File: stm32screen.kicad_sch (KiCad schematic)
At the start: 43 parts, among them J2 GC9A01, J3 Oil temp sensor, J4 pressure sensor, J5 USB_B_Micro, J6 EGT_sensor, SW1 SW_Push, SW2 SW_Push, U1 TS1117BCW-3.3, U2 STM32F407VETx, U3 MAX31856

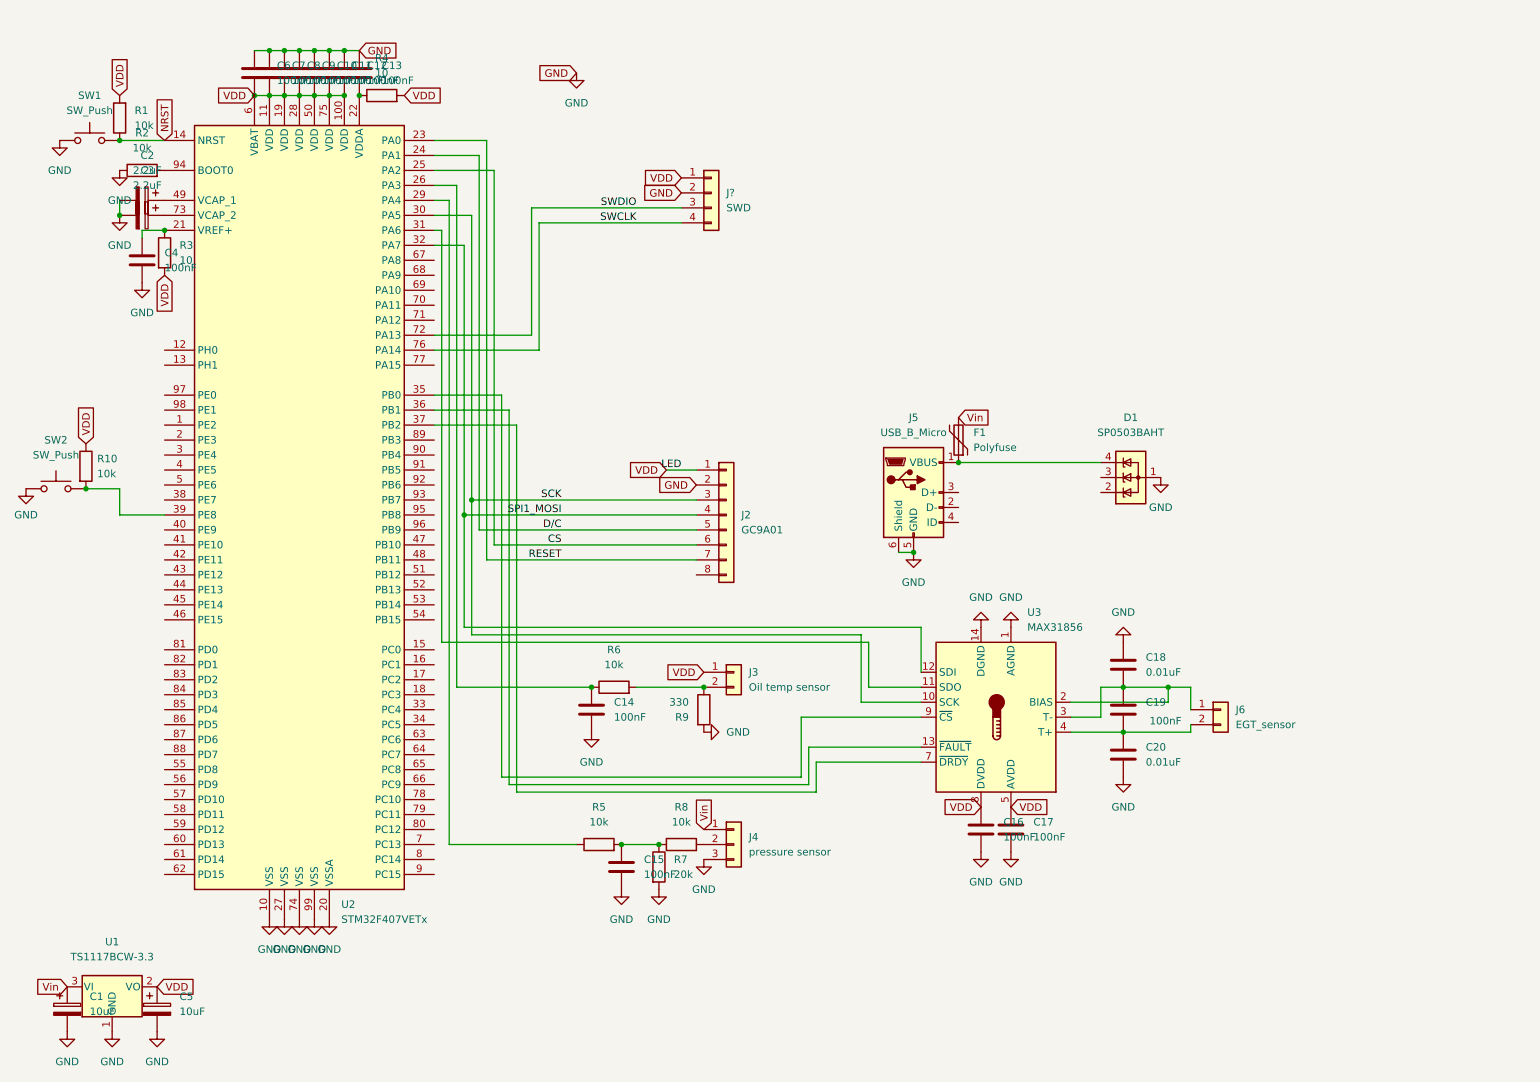
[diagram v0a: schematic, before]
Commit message: Roughing out the PCB.
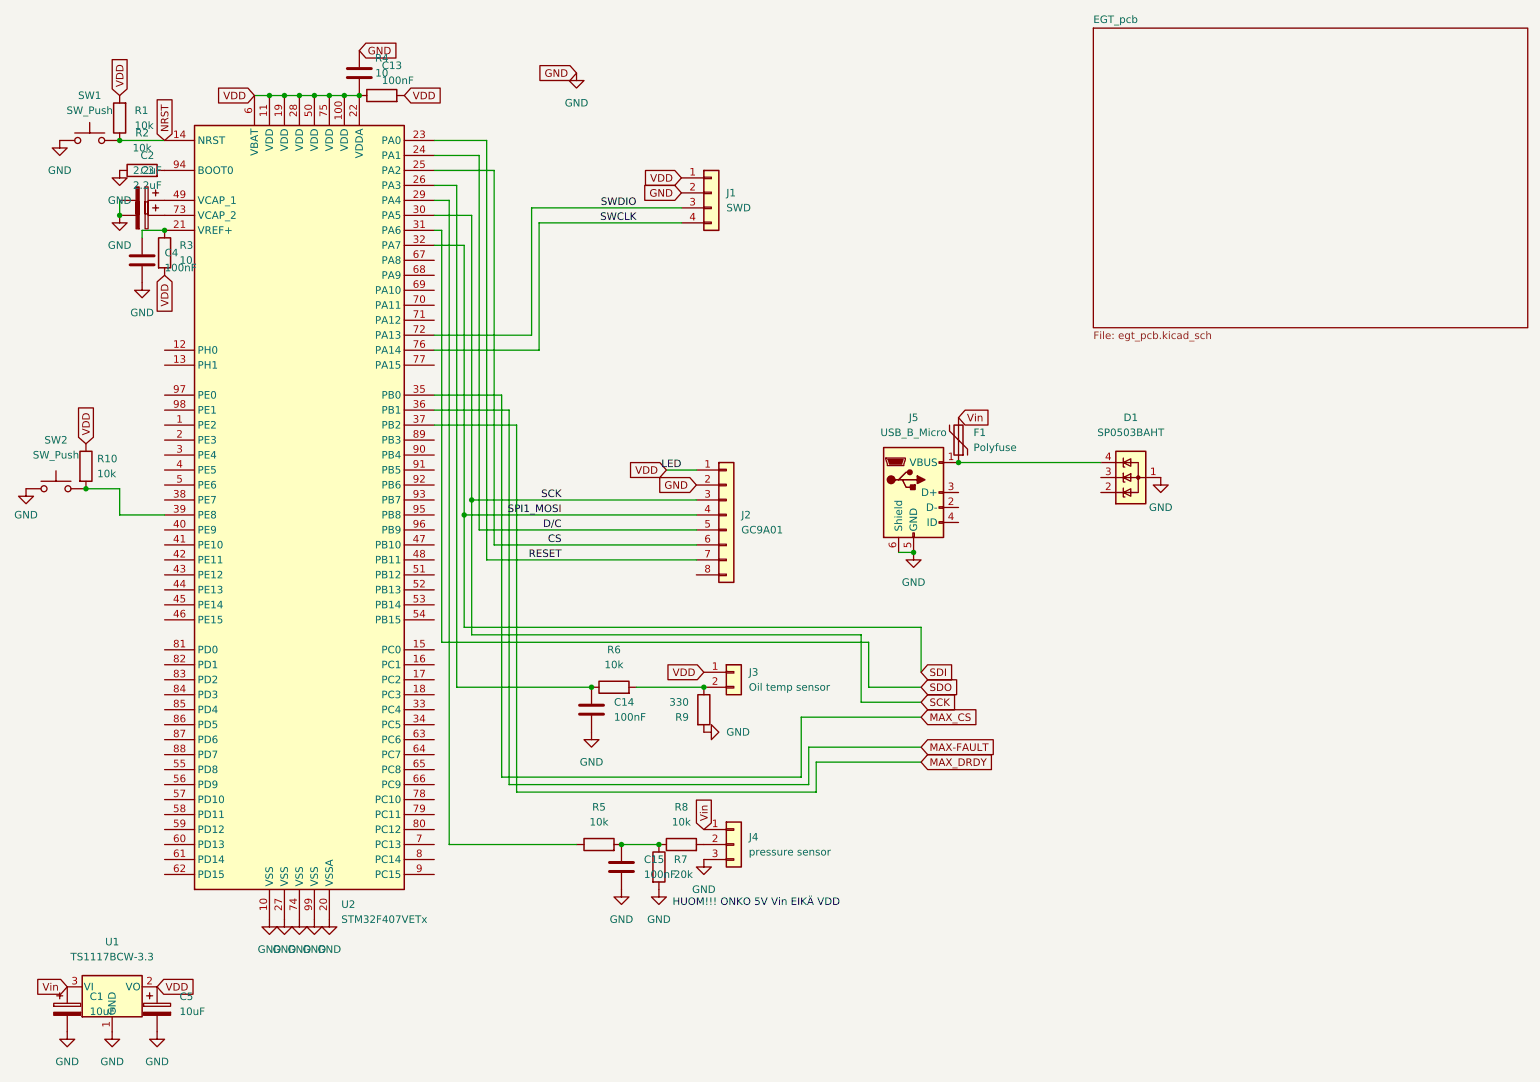
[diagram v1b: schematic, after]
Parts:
- removed C10, C11, C12, C16, C17, C19, C6, C7, C8, C9: 100nF, Capacitor_SMD:C_0805_2012Metric_Pad1.18x1.45mm_HandSolder, symbol Device:C
- removed C18, C20: 0.01uF, Capacitor_SMD:C_0402_1005Metric_Pad0.74x0.62mm_HandSolder, symbol Device:C
- removed J6: EGT_sensor, Connector_JST:JST_XH_B2B-XH-A_1x02_P2.50mm_Vertical, symbol Connector_Generic:Conn_01x02
- removed U3: MAX31856, Package_SO:TSSOP-14_4.4x5mm_P0.65mm, symbol Sensor_Temperature:MAX31856
- gave numbers to parts that had none: 1
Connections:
- net VDD: now also C13.2, R4.1, U2.22 (VDDA)
- net SDO: now reaches U2.31 (PA6)
- net MAX_CS: now reaches U2.35 (PB0)
- net MAX-FAULT: now reaches U2.36 (PB1)
- net MAX_DRDY: now reaches U2.37 (PB2)
- net SPI1_MOSI renamed SDI
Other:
- added sheet EGT_pcb (egt_pcb.kicad_sch)
- note added: "HUOM!!! ONKO 5V Vin EIKÄ VDD"

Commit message: Added a status LED
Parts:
- added D2: LED, LED_SMD:LED_0603_1608Metric_Pad1.05x0.95mm_HandSolder, symbol Device:LED
- added R11: 68, Resistor_SMD:R_0603_1608Metric_Pad0.98x0.95mm_HandSolder, symbol Device:R
- J1: footprint (none) -> Connector_PinHeader_2.54mm:PinHeader_1x04_P2.54mm_Vertical
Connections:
- net GND: now also R11.1
- net VDD: now also D2.2 (A)
- new net: D2.1 (K), R11.2
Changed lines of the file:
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@@
+		)
+	)
+	(global_label "GND"
+		(shape input)
+		(at 130.81 72.39 180)
+		(fields_autoplaced yes)
+		(effects
+			(font
+				(size 1.27 1.27)
+			)
+			(justify right)
+		)
+		(property "Intersheetrefs" "${INTERSHEET_REFS}"
+			(at 123.9543 72.39 0)
+			(effects
+				(font
+					(size 1.27 1.27)
+				)
+				(justify right)
+				(hide yes)
+			)
 		)
 	)
@@
 		)
 	)
+	(global_label "VDD"
+		(shape input)
+		(at 146.05 72.39 0)
+		(fields_autoplaced yes)
+		(effects
+			(font
+				(size 1.27 1.27)
+			)
+			(justify left)
+		)
+		(property "Intersheetrefs" "${INTERSHEET_REFS}"
+			(at 152.6638 72.39 0)
+			(effects
+				(font
+					(size 1.27 1.27)
+				)
+				(justify left)
+				(hide yes)
+			)
+		)
+	)
 	(global_label "SDO"
 		(shape input)
@@
 			)
 		)
-		(property "Footprint" ""
+		(property "Footprint" "Connector_PinHeader_2.54mm:PinHeader_1x04_P2.54mm_Vertical"
 			(at 134.62 43.18 0)
 			(effects
@@
 	)
 	(symbol
+		(lib_id "Device:LED")
+		(at 142.24 72.39 0)
+		(unit 1)
+		(exclude_from_sim no)
+		(in_bom yes)
+		(on_board yes)
+		(dnp no)
+		(fields_autoplaced yes)
+		(property "Reference" "D2"
+			(at 140.6525 66.04 0)
+			(effects
+				(font
+					(size 1.27 1.27)
+				)
+			)
+		)
+		(property "Value" "LED"
+			(at 140.6525 68.58 0)
+			(effects
+				(font
+					(size 1.27 1.27)
+				)
+			)
+		)
+		(property "Footprint" "LED_SMD:LED_0603_1608Metric_Pad1.05x0.95mm_HandSolder"
+			(at 142.24 72.39 0)
+			(effects
+				(font
+					(size 1.27 1.27)
+				)
+				(hide yes)
+			)
+		)
+		(property "Datasheet" "~"
+			(at 142.24 72.39 0)
+			(effects
+				(font
+					(size 1.27 1.27)
+				)
+				(hide yes)
+			)
+		)
+		(property "Description" "Light emitting diode"
+			(at 142.24 72.39 0)
+			(effects
+				(font
+					(size 1.27 1.27)
+				)
+				(hide yes)
+			)
+		)
+		(property "Sim.Pins" "1=K 2=A"
+			(at 142.24 72.39 0)
+			(effects
+				(font
+					(size 1.27 1.27)
+				)
+				(hide yes)
+			)
+		)
+		(pin "1"
+		)
+		(pin "2"
+		)
+		(instances
+			(project ""
+				(path "/dd9634c9-b7ae-401f-800b-241ca4b8e751"
+					(reference "D2")
+					(unit 1)
+				)
+			)
+		)
+	)
+	(symbol
 		(lib_id "power:GND")
 		(at 111.76 22.86 0)
@@
 					(unit 1)
 				)
+			)
+		)
+	)
+	(symbol
+		(lib_id "Device:R")
+		(at 134.62 72.39 90)
+		(unit 1)
+		(exclude_from_sim no)
+		(in_bom yes)
+		(on_board yes)
+		(dnp no)
+		(fields_autoplaced yes)
+		(property "Reference" "R11"
+			(at 134.62 66.04 90)
+			(effects
+				(font
+					(size 1.27 1.27)
+				)
+			)
+		)
+		(property "Value" "68"
+			(at 134.62 68.58 90)
+			(effects
+				(font
+					(size 1.27 1.27)
+				)
+			)
+		)
+		(property "Footprint" "Resistor_SMD:R_0603_1608Metric_Pad0.98x0.95mm_HandSolder"
+			(at 134.62 74.168 90)
+			(effects
+				(font
+					(size 1.27 1.27)
+				)
+				(hide yes)
+			)
+		)
+		(property "Datasheet" "~"
+			(at 134.62 72.39 0)
+			(effects
+				(font
+					(size 1.27 1.27)
+				)
+				(hide yes)
+			)
+		)
+		(property "Description" "Resistor"
+			(at 134.62 72.39 0)
+			(effects
+				(font
+					(size 1.27 1.27)
+				)
+				(hide yes)
+			)
+		)
+		(pin "1"
+		)
+		(pin "2"
+		)
+		(instances
+			(project ""
+				(path "/dd9634c9-b7ae-401f-800b-241ca4b8e751"
+					(reference "R11")
+					(unit 1)
+				)

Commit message: Optimized PCB layout. Added images
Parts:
- J2: footprint Connector_PinHeader_2.54mm:PinHeader_1x08_P2.54mm_Vertical -> Connector_JST:JST_PH_B7B-PH-K_1x07_P2.00mm_Vertical
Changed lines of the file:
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@@
+	)
+	(junction
+		(at 187.96 88.9)
+		(diameter 0)
+		(color 0 0 0 0)
 	)
 	(junction
@@
 	(wire
 		(pts
+			(xy 187.96 88.9) (xy 200.66 88.9)
+		)
+		(stroke
+			(width 0)
+			(type default)
+		)
+	)
+	(wire
+		(pts
 			(xy 160.02 129.54) (xy 160.02 118.11)
 		)
@@
 	(wire
 		(pts
-			(xy 176.53 88.9) (xy 200.66 88.9)
+			(xy 187.96 80.01) (xy 187.96 88.9)
+		)
+		(stroke
+			(width 0)
+			(type default)
+		)
+	)
+	(wire
+		(pts
+			(xy 176.53 88.9) (xy 187.96 88.9)
 		)
 		(stroke
@@
 			)
 		)
-		(property "Footprint" "Connector_PinHeader_2.54mm:PinHeader_1x08_P2.54mm_Vertical"
+		(property "Footprint" "Connector_JST:JST_PH_B7B-PH-K_1x07_P2.00mm_Vertical"
 			(at 137.16 97.79 0)
 			(effects

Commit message: Changed PCB size to 23mm radius, rearranged parts to fit
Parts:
- removed J5: USB_B_Micro, Connector_USB:USB_Micro-B_Amphenol_10118194_Horizontal, symbol Connector:USB_B_Micro
- added J5: POWER IN, Connector_JST:JST_XH_B2B-XH-A_1x02_P2.50mm_Vertical, symbol Connector_Generic:Conn_01x02
- SW1: footprint Button_Switch_THT:SW_PUSH_6mm -> Button_Switch_SMD:SW_Push_1P1T_NO_CK_KSC9xxG
- SW2: footprint Connector_PinHeader_2.54mm:PinHeader_1x02_P2.54mm_Vertical -> Button_Switch_SMD:SW_Push_1P1T_NO_CK_KSC9xxG
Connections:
- net GND: now also J5.1 (Pin_1)
- net at D1.4 (K), F1.1: now also J5.2 (Pin_2)
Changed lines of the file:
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@@
 	)
 	(junction
-		(at 187.96 88.9)
-		(diameter 0)
-		(color 0 0 0 0)
-	)
-	(junction
 		(at 64.77 26.67)
 		(diameter 0)
@@
 	)
 	(junction
-		(at 168.91 104.14)
-		(diameter 0)
-		(color 0 0 0 0)
-	)
-	(junction
 		(at 67.31 26.67)
 		(diameter 0)
@@
 	(wire
 		(pts
-			(xy 187.96 88.9) (xy 200.66 88.9)
-		)
-		(stroke
-			(width 0)
-			(type default)
-		)
-	)
-	(wire
-		(pts
 			(xy 160.02 129.54) (xy 160.02 118.11)
 		)
@@
 	(wire
 		(pts
-			(xy 166.37 104.14) (xy 168.91 104.14)
-		)
-		(stroke
-			(width 0)
-			(type default)
-		)
-	)
-	(wire
-		(pts
 			(xy 161.29 119.38) (xy 161.29 127)
 		)
@@
 	(wire
 		(pts
-			(xy 88.9 119.38) (xy 161.29 119.38)
+			(xy 176.53 88.9) (xy 167.64 88.9)
 		)
 		(stroke
@@
 	(wire
 		(pts
-			(xy 187.96 80.01) (xy 187.96 88.9)
+			(xy 88.9 119.38) (xy 161.29 119.38)
 		)
 		(stroke
@@
 	(wire
 		(pts
-			(xy 176.53 88.9) (xy 187.96 88.9)
+			(xy 176.53 88.9) (xy 200.66 88.9)
 		)
 		(stroke
@@
 	(wire
 		(pts
+			(xy 167.64 88.9) (xy 167.64 90.17)
+		)
+		(stroke
+			(width 0)
+			(type default)
+		)
+	)
+	(wire
+		(pts
 			(xy 101.6 82.55) (xy 87.63 82.55)
 		)
@@
 	)
 	(symbol
-		(lib_id "Connector:USB_B_Micro")
-		(at 168.91 93.98 0)
-		(unit 1)
-		(exclude_from_sim no)
-		(in_bom yes)
-		(on_board yes)
-		(dnp no)
-		(fields_autoplaced yes)
-		(property "Reference" "J5"
-			(at 168.91 81.28 0)
-			(effects
-				(font
-					(size 1.27 1.27)
-				)
-			)
-		)
-		(property "Value" "USB_B_Micro"
-			(at 168.91 83.82 0)
-			(effects
-				(font
-					(size 1.27 1.27)
-				)
-			)
-		)
-		(property "Footprint" "Connector_USB:USB_Micro-B_Amphenol_10118194_Horizontal"
-			(at 172.72 95.25 0)
-			(effects
-				(font
-					(size 1.27 1.27)
-				)
-				(hide yes)
-			)
-		)
-		(property "Datasheet" "~"
-			(at 172.72 95.25 0)
-			(effects
-				(font
-					(size 1.27 1.27)
-				)
-				(hide yes)
-			)
-		)
-		(property "Description" ""
-			(at 168.91 93.98 0)
-			(effects
-				(font
-					(size 1.27 1.27)
-				)
-			)
-		)
-		(pin "1"
-		)
-		(pin "2"
-		)
-		(pin "3"
-		)
-		(pin "4"
-		)
-		(pin "5"
-		)
-		(pin "6"
-		)
-		(instances
-			(project ""
-				(path "/dd9634c9-b7ae-401f-800b-241ca4b8e751"
-					(reference "J5")
-					(unit 1)
-				)
-			)
-		)
-	)
-	(symbol
 		(lib_id "Switch:SW_Push")
 		(at 29.21 34.29 0)
@@
 			)
 		)
-		(property "Footprint" "Button_Switch_THT:SW_PUSH_6mm"
+		(property "Footprint" "Button_Switch_SMD:SW_Push_1P1T_NO_CK_KSC9xxG"
 			(at 29.21 29.21 0)
 			(effects
@@
 	(symbol
 		(lib_id "power:GND")
-		(at 168.91 104.14 0)
-		(unit 1)
-		(exclude_from_sim no)
-		(in_bom yes)
-		(on_board yes)
-		(dnp no)
-		(fields_autoplaced yes)
-		(property "Reference" "#PWR019"
-			(at 168.91 110.49 0)
-			(effects
-				(font
-					(size 1.27 1.27)
-				)
-				(hide yes)
-			)
-		)
-		(property "Value" "GND"
-			(at 168.91 109.22 0)
-			(effects
-				(font
-					(size 1.27 1.27)
-				)
-			)
-		)
-		(property "Footprint" ""
-			(at 168.91 104.14 0)
-			(effects
-				(font
-					(size 1.27 1.27)
-				)
-				(hide yes)
-			)
-		)
-		(property "Datasheet" ""
-			(at 168.91 104.14 0)
-			(effects
-				(font
-					(size 1.27 1.27)
-				)
-				(hide yes)
-			)
-		)
-		(property "Description" ""
-			(at 168.91 104.14 0)
-			(effects
-				(font
-					(size 1.27 1.27)
-				)
-			)
-		)
-		(pin "1"
-		)
-		(instances
-			(project ""
-				(path "/dd9634c9-b7ae-401f-800b-241ca4b8e751"
-					(reference "#PWR019")
-					(unit 1)
-				)
-			)
-		)
-	)
-	(symbol
-		(lib_id "power:GND")
 		(at 33.02 185.42 0)
 		(unit 1)
@@
 			)
 		)
-		(property "Footprint" "Connector_PinHeader_2.54mm:PinHeader_1x02_P2.54mm_Vertical"
+		(property "Footprint" "Button_Switch_SMD:SW_Push_1P1T_NO_CK_KSC9xxG"
 			(at 23.495 88.265 0)
 			(effects
@@
 	)
 	(symbol
+		(lib_id "power:GND")
+		(at 167.64 92.71 0)
+		(unit 1)
+		(exclude_from_sim no)
+		(in_bom yes)
+		(on_board yes)
+		(dnp no)
+		(property "Reference" "#PWR021"
+			(at 167.64 99.06 0)
+			(effects
+				(font
+					(size 1.27 1.27)
+				)
+				(hide yes)
+			)
+		)
+		(property "Value" "GND"
+			(at 167.6401 96.52 90)
+			(effects
+				(font
+					(size 1.27 1.27)
+				)
+				(justify right)
+			)
+		)
+		(property "Footprint" ""
+			(at 167.64 92.71 0)
+			(effects
+				(font
+					(size 1.27 1.27)
+				)
+				(hide yes)
+			)
+		)
+		(property "Datasheet" ""
+			(at 167.64 92.71 0)
+			(effects
+				(font
+					(size 1.27 1.27)
+				)
+				(hide yes)
+			)
+		)
+		(property "Description" ""
+			(at 167.64 92.71 0)
+			(effects
+				(font
+					(size 1.27 1.27)
+				)
+			)
+		)
+		(pin "1"
+		)
+		(instances
+			(project "stm32screen"
+				(path "/dd9634c9-b7ae-401f-800b-241ca4b8e751"
+					(reference "#PWR021")
+					(unit 1)
+				)
+			)
+		)
+	)
+	(symbol
 		(lib_id "Device:C_Polarized")
 		(at 25.4 181.61 0)
@@
 					(unit 1)
 				)
+			)
+		)
+	)
+	(symbol
+		(lib_id "Connector_Generic:Conn_01x02")
+		(at 162.56 92.71 180)
+		(unit 1)
+		(exclude_from_sim no)
+		(in_bom yes)
+		(on_board yes)
+		(dnp no)
+		(fields_autoplaced yes)
+		(property "Reference" "J5"
+			(at 162.56 83.82 0)
+			(effects
+				(font
+					(size 1.27 1.27)
+				)
+			)
+		)
+		(property "Value" "POWER IN"
+			(at 162.56 86.36 0)
+			(effects
+				(font
+					(size 1.27 1.27)
+				)
+			)
+		)
+		(property "Footprint" "Connector_JST:JST_XH_B2B-XH-A_1x02_P2.50mm_Vertical"
+			(at 162.56 92.71 0)
+			(effects
+				(font
+					(size 1.27 1.27)
+				)
+				(hide yes)
+			)
+		)
+		(property "Datasheet" "~"
+			(at 162.56 92.71 0)
+			(effects
+				(font
+					(size 1.27 1.27)
+				)
+				(hide yes)
+			)
+		)
+		(property "Description" "Generic connector, single row, 01x02, script generated (kicad-library-utils/schlib/autogen/connector/)"
+			(at 162.56 92.71 0)
+			(effects
+				(font
+					(size 1.27 1.27)
+				)
+				(hide yes)
+			)
+		)
+		(pin "2"
+		)
+		(pin "1"
+		)
+		(instances
+			(project ""
+				(path "/dd9634c9-b7ae-401f-800b-241ca4b8e751"
+					(reference "J5")
+					(unit 1)
+				)
